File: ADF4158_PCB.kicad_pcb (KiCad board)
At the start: 2 copper layers, 55 x 25 mm, 80 parts, among them J1 Conn_02x04_Odd_Even, J2 SMA, J3 SMA, Q1 DMP3099L-13, Q2 2N7002BK, U1 LP2985-10.0, U2 TLV74130P, U3 TLV74033P, U4 HMC391, U5 AD8065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

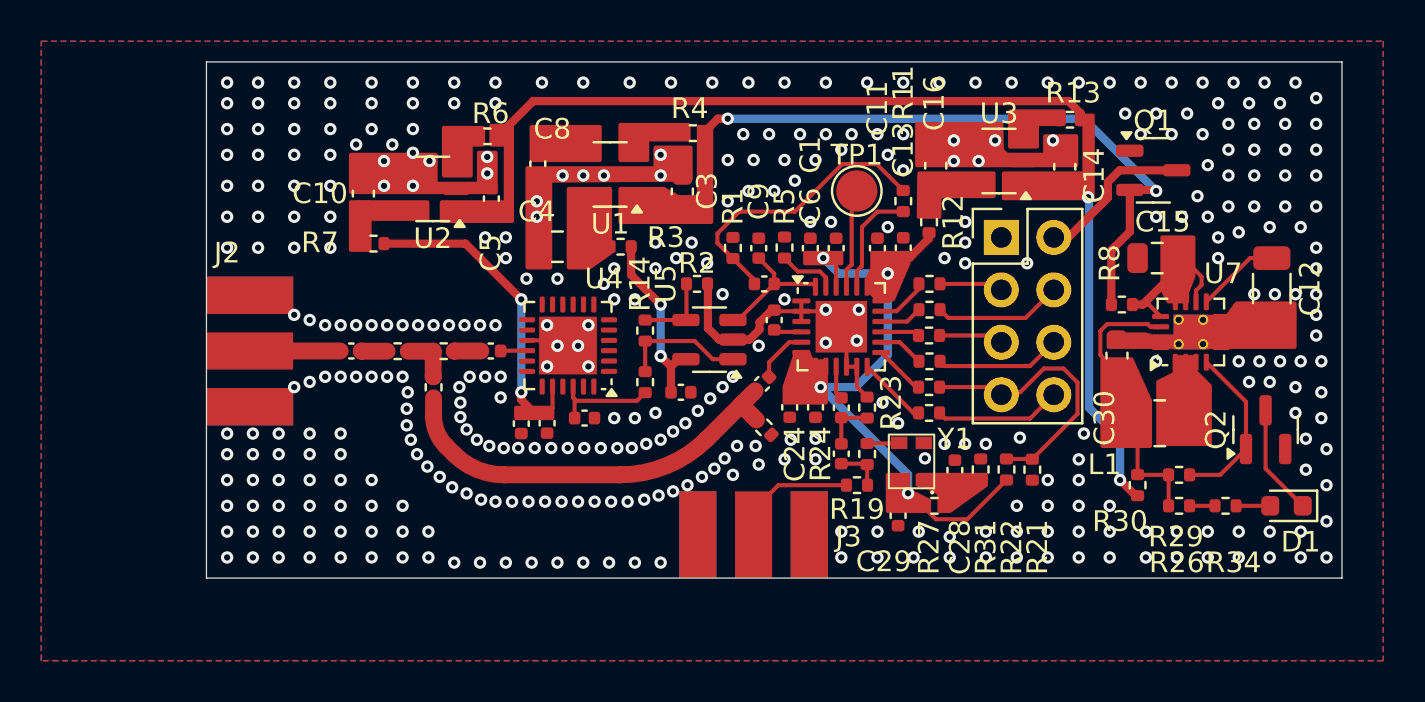
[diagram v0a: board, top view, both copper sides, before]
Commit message: some minor PCB improvements
- Do not route 3V0 trace on back right below HMC391 RF out
- Add multiple vias for 5V and 12V power traces

Signed-off-by: Daniel Estévez <daniel@destevez.net>
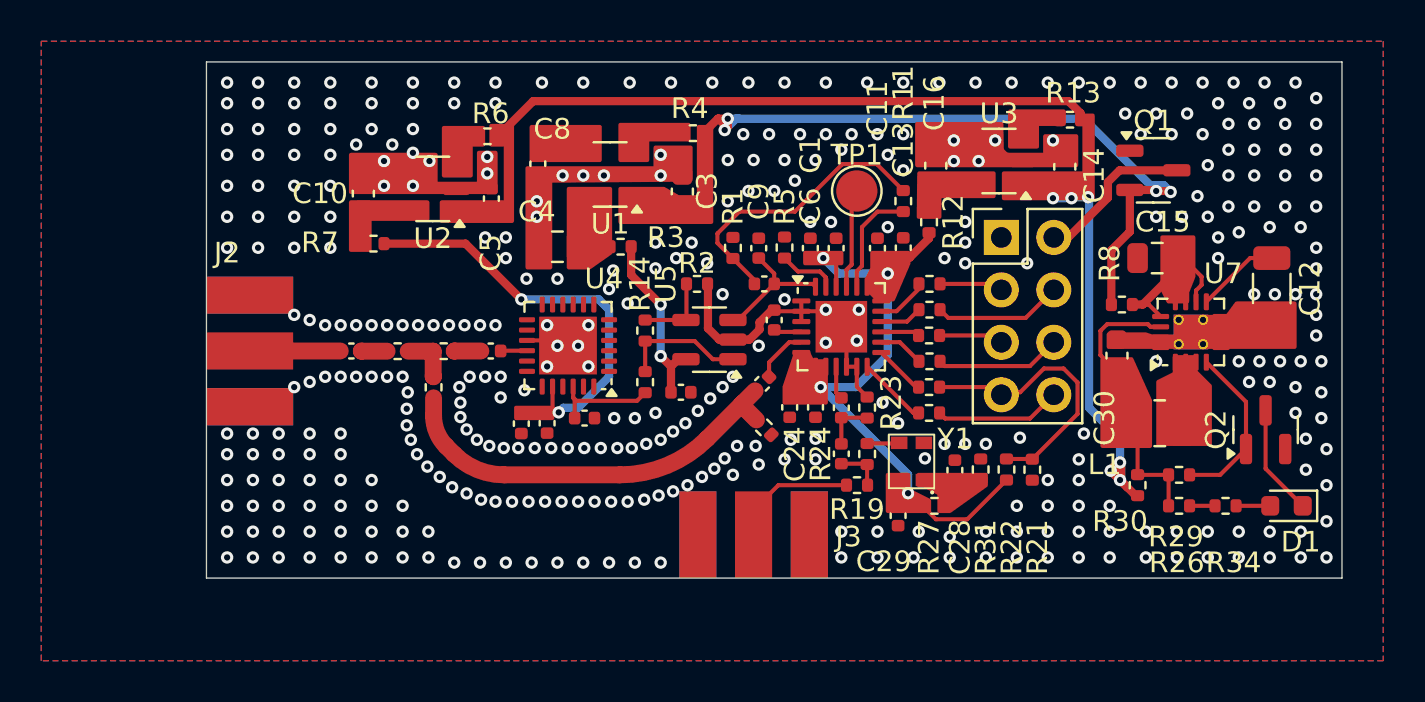
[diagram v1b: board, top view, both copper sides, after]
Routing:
- net +3V0: track 14.9 -> 20.6 mm
- net +12V: track 30.9 -> 34.9 mm, vias 2 -> 4
- net +5V: track 46.6 -> 48.7 mm, vias 2 -> 6

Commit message: switch to 4-layer 1.6mm PCB stackup from JLCPCB
- By recommendation of reviewers, use a 4-layer 1.6 PCB stackup from
JLCPCB that gives 0.6 mm 50 ohm CPWG traces on the top layer.

- Use an SMA connector with a thin pin for the RF output.

- Remove 51 ohm resistor loading the ADF4518 PCB. This is believed
to be a mistake in the evaluation board schematic.

- Add M2 mounting holes to the board corners.

- Connect NC pins of HMC391 to GND as in the evaluation board.

Signed-off-by: Daniel Estévez <daniel@destevez.net>
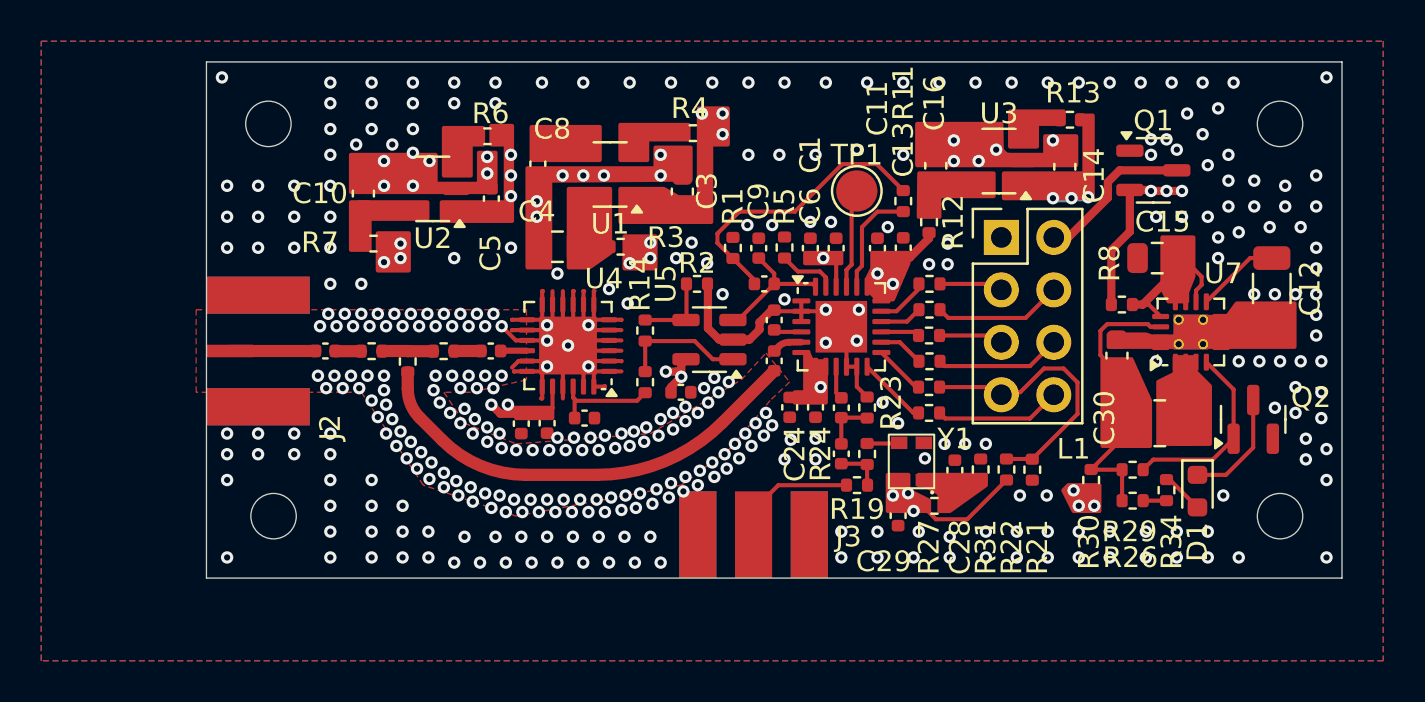
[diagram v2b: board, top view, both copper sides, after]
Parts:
- removed R15: 51, Resistor_SMD:R_0402_1005Metric
- added H1: MountingHole, MountingHole:MountingHole_2.2mm_M2, F.Cu at (125.5, 91.0)
- added H2: MountingHole, MountingHole:MountingHole_2.2mm_M2, F.Cu at (174.5, 91.0)
- added H3: MountingHole, MountingHole:MountingHole_2.2mm_M2, F.Cu at (125.8, 110.0)
- added H4: MountingHole, MountingHole:MountingHole_2.2mm_M2, F.Cu at (174.5, 110.0)
- J2: footprint ADF4158_HMC391_PCB:WRL-23187 -> ADF4158_HMC391_PCB:2484637-1
- moved D1 4.37 mm to (170.5, 108.8), turned to -90 degrees
- moved R34 2.96 mm to (169.0, 108.7), turned to -90 degrees
- moved R26 2.26 mm to (167.4, 109.2)
- moved R29 2.26 mm to (167.4, 107.8)
- moved R30 2.26 mm to (165.3, 108.2)
- moved J2 2.10 mm to (122.5, 102.0)
- moved R18 1.77 mm to (132.2, 102.5)
- moved C21 1.26 mm to (128.3, 102.0)
- moved R16 1.26 mm to (130.5, 102.0)
- moved C17 1.26 mm to (150.0, 102.5), turned to -90 degrees
- moved Q2 0.78 mm to (173.2, 105.3)
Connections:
- U4 pad 1: unconnected-(U4-NC-Pad1) -> GND
- U4 pad 10: unconnected-(U4-NC-Pad1)_16 -> GND
- U4 pad 11: unconnected-(U4-NC-Pad1)_6 -> GND
- U4 pad 12: unconnected-(U4-NC-Pad1)_18 -> GND
- U4 pad 13: unconnected-(U4-NC-Pad1)_7 -> GND
- U4 pad 14: unconnected-(U4-NC-Pad1)_13 -> GND
- U4 pad 17: unconnected-(U4-NC-Pad1)_2 -> GND
- U4 pad 18: unconnected-(U4-NC-Pad1)_5 -> GND
- U4 pad 19: unconnected-(U4-NC-Pad1)_12 -> GND
- U4 pad 2: unconnected-(U4-NC-Pad1)_15 -> GND
- U4 pad 21: unconnected-(U4-NC-Pad1)_8 -> GND
- U4 pad 23: unconnected-(U4-NC-Pad1)_4 -> GND
- U4 pad 24: unconnected-(U4-NC-Pad1)_11 -> GND
- U4 pad 3: unconnected-(U4-NC-Pad1)_9 -> GND
- U4 pad 4: unconnected-(U4-NC-Pad1)_14 -> GND
- U4 pad 5: unconnected-(U4-NC-Pad1)_19 -> GND
- U4 pad 6: unconnected-(U4-NC-Pad1)_1 -> GND
- U4 pad 7: unconnected-(U4-NC-Pad1)_17 -> GND
- U4 pad 8: unconnected-(U4-NC-Pad1)_10 -> GND
- U4 pad 9: unconnected-(U4-NC-Pad1)_3 -> GND
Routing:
- net +5V: track 48.7 -> 3.41 mm, vias 6 -> 9
- net GND: track 18.2 -> 51.9 mm, vias 375 -> 370
- net +12V: track 34.9 -> 8.47 mm, vias 4 -> 6
- net +3V3: track 26.7 -> 8.52 mm, vias 4 -> 7
- net +3V0: track 20.6 -> 3.72 mm, vias 2 -> 5
- net +10V: track 8.29 -> 2.85 mm, vias 2 -> 5
- net Net-(C17-Pad2): track 20.3 -> 22.1 mm
- net Net-(U6-RFINA): track 2.67 -> 1.48 mm
- net Net-(Q2-G): track 8.25 -> 9.26 mm
- net Net-(U7-VOS): track 11.4 -> 12.3 mm
- added copper zone on In2.Cu, net +10V
- added copper zone on In2.Cu, net +12V
- added copper zone on In2.Cu, net +3V0
- added copper zone on In2.Cu, net +3V3
- added copper zone on In2.Cu, net +5V
- added copper zone on In1.Cu, net GND
- added copper zone on In2.Cu, net GND
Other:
- copper layers 2 -> 4
- board text added: "0.02"
- board text added: "0.124 mm"
- board text added: "0.2104 mm"
- board text added: "0.7 mm"
- board text added: "1.4996 mm"
- board text added: "2116"
- board text added: "4"
- board text added: "4.16"
- board text added: "4.4"
- board text added: "7628"
- board text added: "Dielectric 1 (1/2)"
- board text added: "Dielectric 2"
- board text added: "Dielectric 3 (1/2)"
- board text added: "HAL SnPb"
- board text added: "In1.Cu"
- board text added: "In2.Cu"
- board text added: "prepreg"
- board text removed: "0.022"
- board text removed: "0.5 mm"
- board text removed: "0.6004 mm"
- board text removed: "2"
- board text removed: "Dielectric"
- board text removed: "HAL lead-free"

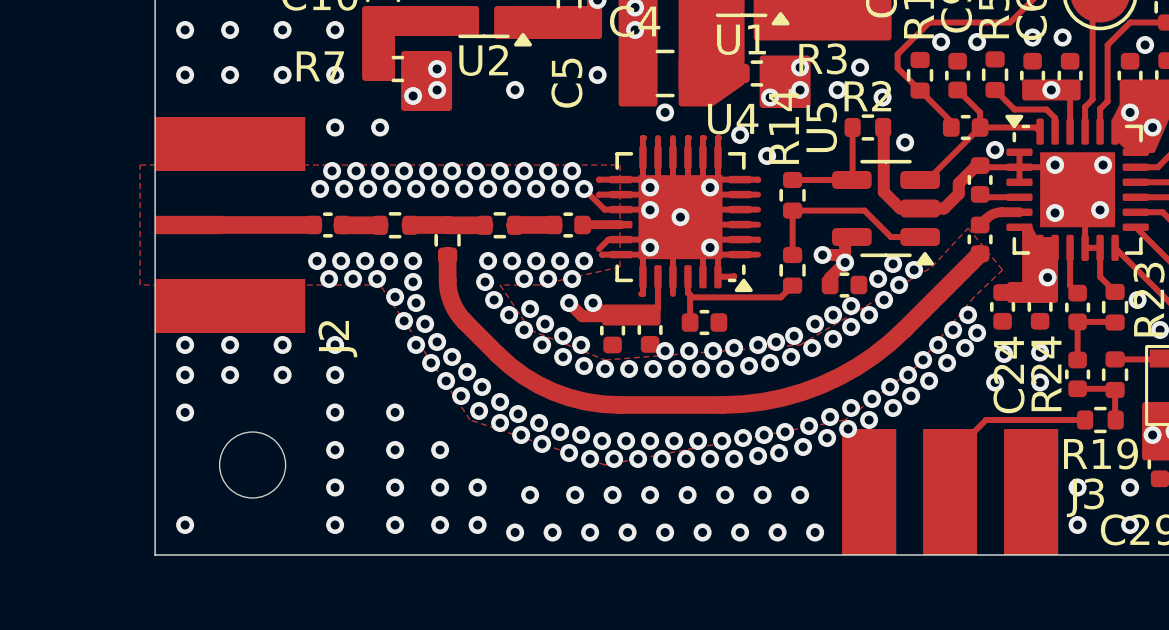
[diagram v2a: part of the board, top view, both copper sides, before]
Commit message: switch from JLC04161H-2116D to JLC04161H-7628 stackup
Unfortunately the 2116D stackup that I used to get 50 ohm traces
of approximately 0.6 mm now costs a huge amount. Use instead the
7628 stackup, which is JLCPCB's cheap/default/recommended stackup.
This gives 0.3658 mm 50 ohm traces, which is not ideal for matching
with 0402 parts.

Signed-off-by: Daniel Estévez <daniel@destevez.net>
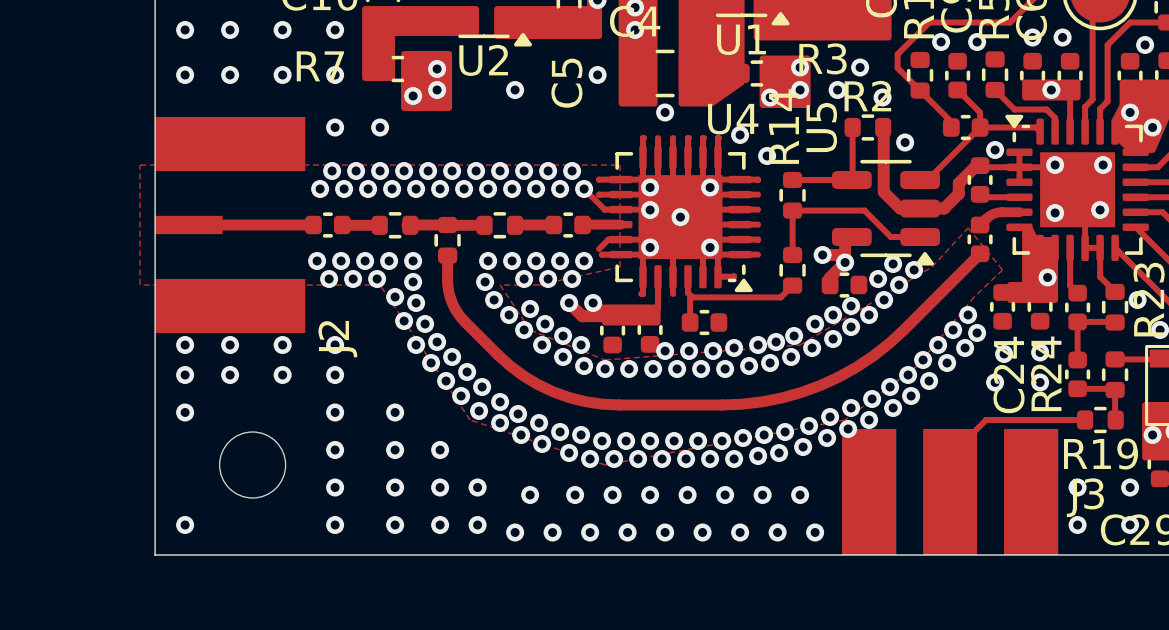
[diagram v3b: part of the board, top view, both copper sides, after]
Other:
- board text added: "1.065 mm"
- board text added: "Dielectric 1"
- board text added: "Dielectric 3"
- board text removed: "0.124 mm"
- board text removed: "0.7 mm"
- board text removed: "2116"
- board text removed: "4.16"
- board text removed: "Dielectric 1 (1/2)"
- board text removed: "Dielectric 3 (1/2)"

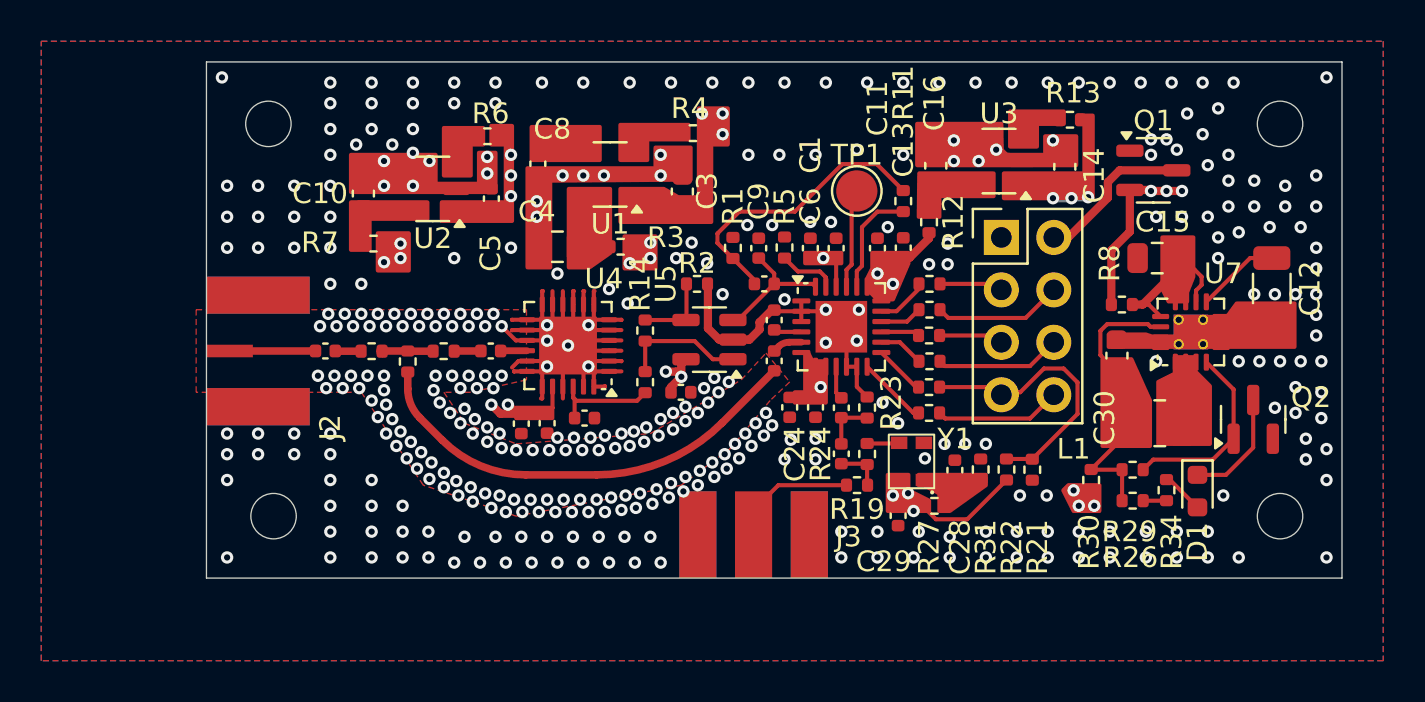
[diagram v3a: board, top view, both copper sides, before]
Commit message: use thermal relief in GND pour
- Use thermal relief in GND pour
- Add vias to SMD GND pads

Signed-off-by: Daniel Estévez <daniel@destevez.net>
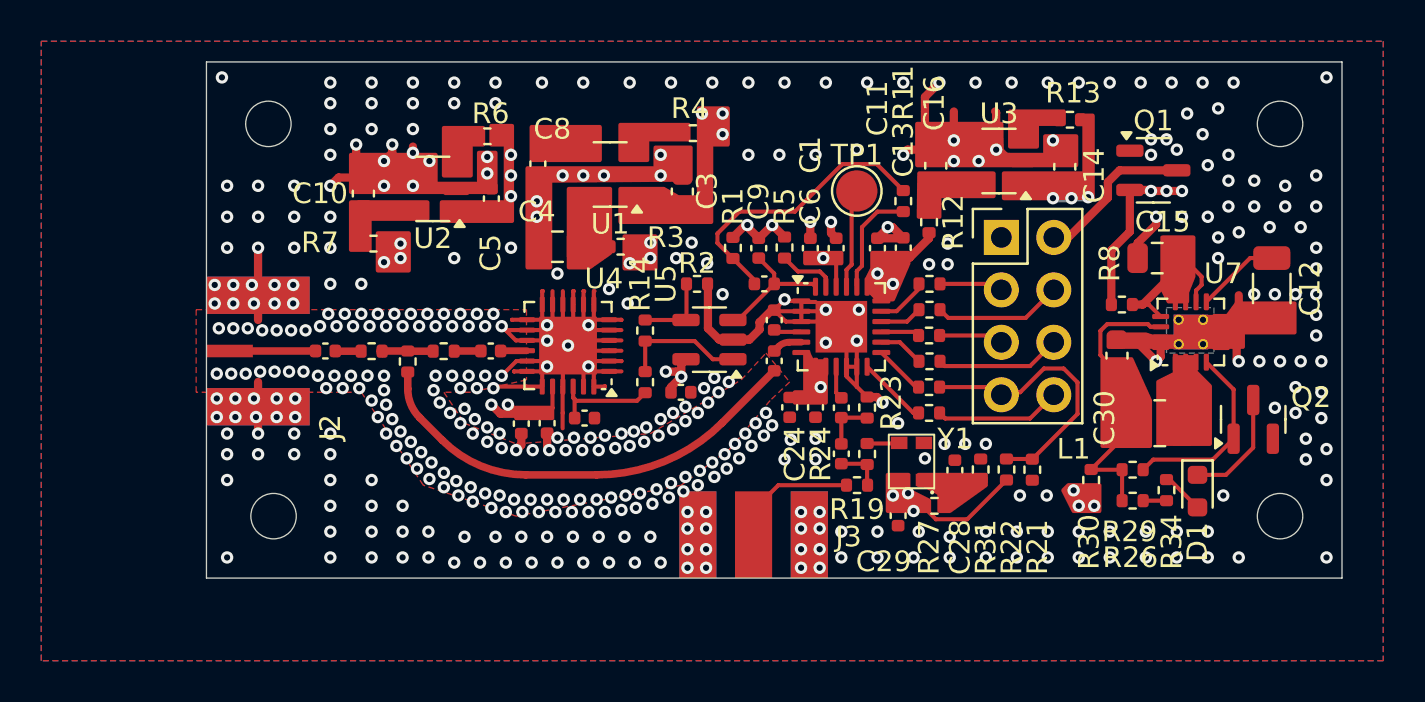
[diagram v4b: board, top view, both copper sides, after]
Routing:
- net GND: track 51.9 -> 99.4 mm, vias 370 -> 420
